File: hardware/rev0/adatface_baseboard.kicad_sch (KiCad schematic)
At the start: 89 parts, among them J1 Conn_01x06_Male, J2 Conn_02x32_Odd_Even, J3 Conn_02x32_Odd_Even, J4 Connector_USB_C_Receptacle_US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, J5 Connector_USB_C_Receptacle_US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, J6 Conn_01x06_Male, J7 Conn_01x26_Male, J8 Conn_01x01_Male, J9 Conn_01x01_Male, U1 PLR135_T8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

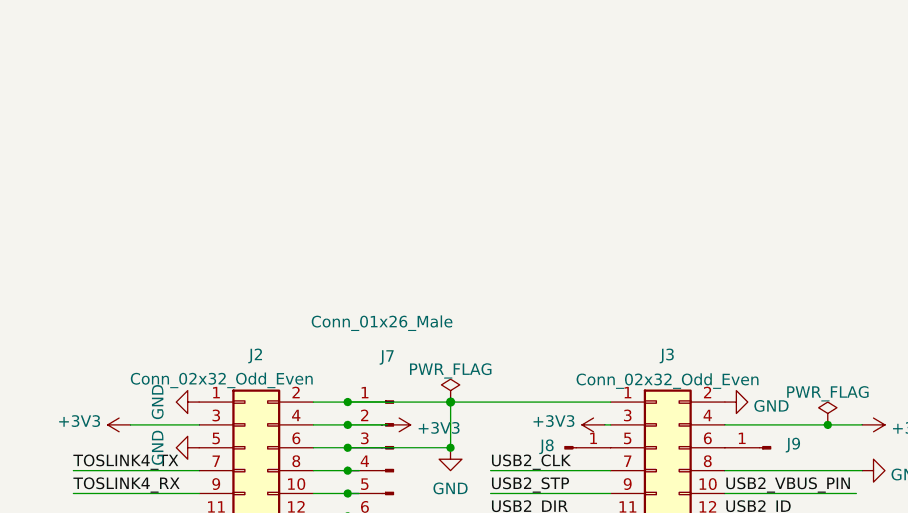
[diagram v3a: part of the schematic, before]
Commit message: baseboard rev0.1: Fix DRC rules with new KiCAD version, length matched USB PHY traces, more ground vias, fix trace spacing, ground headers
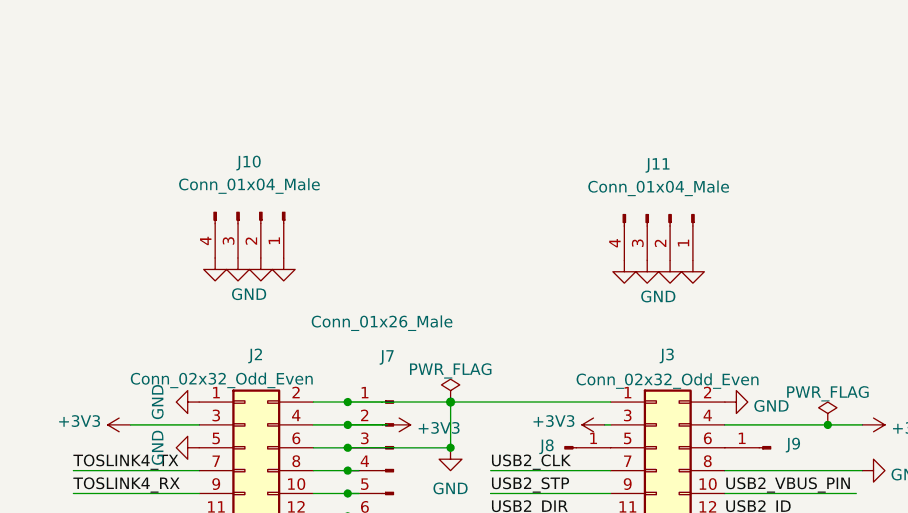
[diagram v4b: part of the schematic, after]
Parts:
- added J10, J11: Conn_01x04_Male, Connector_PinHeader_2.54mm:PinHeader_1x04_P2.54mm_Horizontal, symbol Connector:Conn_01x04_Male
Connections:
- net GND: now also J10.1 (Pin_1), J10.2 (Pin_2), J10.3 (Pin_3), J10.4 (Pin_4), J11.1 (Pin_1), J11.2 (Pin_2), J11.3 (Pin_3), J11.4 (Pin_4)
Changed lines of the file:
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@@
     )
   )
+  (symbol (lib_id "power:GND") (at 145.288 37.338 0) (unit 1)
+    (in_bom yes) (on_board yes)
+    (property "Reference" "#PWR034" (id 0) (at 145.288 43.688 0)
+      (effects (font (size 1.27 1.27)) hide)
+    )
+    (property "Value" "GND" (id 1) (at 144.526 41.402 0)
+      (effects (font (size 1.27 1.27)) (justify left))
+    )
+    (property "Footprint" "" (id 2) (at 145.288 37.338 0)
+      (effects (font (size 1.27 1.27)) hide)
+    )
+    (property "Datasheet" "" (id 3) (at 145.288 37.338 0)
+      (effects (font (size 1.27 1.27)) hide)
+    )
+    (pin "1")
+  )
   (symbol (lib_id "power:GND") (at 250.19 87.63 0) (unit 1)
     (in_bom yes) (on_board yes)
@@
     (pin "1")
   )
+  (symbol (lib_id "power:GND") (at 142.748 37.338 0) (unit 1)
+    (in_bom yes) (on_board yes)
+    (property "Reference" "#PWR033" (id 0) (at 142.748 43.688 0)
+      (effects (font (size 1.27 1.27)) hide)
+    )
+    (property "Value" "GND" (id 1) (at 140.716 41.402 0)
+      (effects (font (size 1.27 1.27)) (justify left) hide)
+    )
+    (property "Footprint" "" (id 2) (at 142.748 37.338 0)
+      (effects (font (size 1.27 1.27)) hide)
+    )
+    (property "Datasheet" "" (id 3) (at 142.748 37.338 0)
+      (effects (font (size 1.27 1.27)) hide)
+    )
+    (pin "1")
+  )
   (symbol (lib_id "power:GND") (at 140.97 53.34 270) (unit 1)
     (in_bom yes) (on_board yes)
@@
     (pin "1")
   )
+  (symbol (lib_id "power:GND") (at 150.368 37.338 0) (unit 1)
+    (in_bom yes) (on_board yes)
+    (property "Reference" "#PWR036" (id 0) (at 150.368 43.688 0)
+      (effects (font (size 1.27 1.27)) hide)
+    )
+    (property "Value" "GND" (id 1) (at 148.336 41.402 0)
+      (effects (font (size 1.27 1.27)) (justify left) hide)
+    )
+    (property "Footprint" "" (id 2) (at 150.368 37.338 0)
+      (effects (font (size 1.27 1.27)) hide)
+    )
+    (property "Datasheet" "" (id 3) (at 150.368 37.338 0)
+      (effects (font (size 1.27 1.27)) hide)
+    )
+    (pin "1")
+  )
   (symbol (lib_id "Connector_Generic:Conn_02x32_Odd_Even") (at 191.77 91.44 0) (unit 1)
     (in_bom yes) (on_board yes) (fields_autoplaced)
@@
     (pin "2")
   )
+  (symbol (lib_id "power:GND") (at 147.828 37.338 0) (unit 1)
+    (in_bom yes) (on_board yes)
+    (property "Reference" "#PWR035" (id 0) (at 147.828 43.688 0)
+      (effects (font (size 1.27 1.27)) hide)
+    )
+    (property "Value" "GND" (id 1) (at 145.796 41.402 0)
+      (effects (font (size 1.27 1.27)) (justify left) hide)
+    )
+    (property "Footprint" "" (id 2) (at 147.828 37.338 0)
+      (effects (font (size 1.27 1.27)) hide)
+    )
+    (property "Datasheet" "" (id 3) (at 147.828 37.338 0)
+      (effects (font (size 1.27 1.27)) hide)
+    )
+    (pin "1")
+  )
   (symbol (lib_id "Device:R_Small") (at 245.11 173.99 270) (unit 1)
     (in_bom yes) (on_board yes)
@@
     (pin "1")
   )
+  (symbol (lib_id "power:GND") (at 188.214 37.592 0) (unit 1)
+    (in_bom yes) (on_board yes)
+    (property "Reference" "#PWR037" (id 0) (at 188.214 43.942 0)
+      (effects (font (size 1.27 1.27)) hide)
+    )
+    (property "Value" "GND" (id 1) (at 186.182 41.656 0)
+      (effects (font (size 1.27 1.27)) (justify left) hide)
+    )
+    (property "Footprint" "" (id 2) (at 188.214 37.592 0)
+      (effects (font (size 1.27 1.27)) hide)
+    )
+    (property "Datasheet" "" (id 3) (at 188.214 37.592 0)
+      (effects (font (size 1.27 1.27)) hide)
+    )
+    (pin "1")
+  )
   (symbol (lib_id "Connector:TestPoint") (at 374.65 173.99 270) (unit 1)
     (in_bom yes) (on_board yes) (fields_autoplaced)
@@
     (pin "1")
   )
+  (symbol (lib_id "power:GND") (at 193.294 37.592 0) (unit 1)
+    (in_bom yes) (on_board yes)
+    (property "Reference" "#PWR039" (id 0) (at 193.294 43.942 0)
+      (effects (font (size 1.27 1.27)) hide)
+    )
+    (property "Value" "GND" (id 1) (at 191.262 41.656 0)
+      (effects (font (size 1.27 1.27)) (justify left) hide)
+    )
+    (property "Footprint" "" (id 2) (at 193.294 37.592 0)
+      (effects (font (size 1.27 1.27)) hide)
+    )
+    (property "Datasheet" "" (id 3) (at 193.294 37.592 0)
+      (effects (font (size 1.27 1.27)) hide)
+    )
+    (pin "1")
+  )
   (symbol (lib_id "Device:C_Small") (at 278.13 90.17 180) (unit 1)
     (in_bom yes) (on_board yes)
@@
     (pin "S1")
   )
+  (symbol (lib_id "power:GND") (at 195.834 37.592 0) (unit 1)
+    (in_bom yes) (on_board yes)
+    (property "Reference" "#PWR040" (id 0) (at 195.834 43.942 0)
+      (effects (font (size 1.27 1.27)) hide)
+    )
+    (property "Value" "GND" (id 1) (at 193.802 41.656 0)
+      (effects (font (size 1.27 1.27)) (justify left) hide)
+    )
+    (property "Footprint" "" (id 2) (at 195.834 37.592 0)
+      (effects (font (size 1.27 1.27)) hide)
+    )
+    (property "Datasheet" "" (id 3) (at 195.834 37.592 0)
+      (effects (font (size 1.27 1.27)) hide)
+    )
+    (pin "1")
+  )
   (symbol (lib_id "Device:LED_Small") (at 251.46 173.99 180) (unit 1)
     (in_bom yes) (on_board yes)
@@
     (pin "2")
   )
+  (symbol (lib_id "Connector:Conn_01x04_Male") (at 193.294 32.512 270) (unit 1)
+    (in_bom yes) (on_board yes) (fields_autoplaced)
+    (property "Reference" "J11" (id 0) (at 192.024 26.924 90))
+    (property "Value" "Conn_01x04_Male" (id 1) (at 192.024 29.464 90))
+    (property "Footprint" "Connector_PinHeader_2.54mm:PinHeader_1x04_P2.54mm_Horizontal" (id 2) (at 193.294 32.512 0)
+      (effects (font (size 1.27 1.27)) hide)
+    )
+    (property "Datasheet" "~" (id 3) (at 193.294 32.512 0)
+      (effects (font (size 1.27 1.27)) hide)
+    )
+    (pin "1")
+    (pin "2")
+    (pin "3")
+    (pin "4")
+  )
+  (symbol (lib_id "Connector:Conn_01x04_Male") (at 147.828 32.258 270) (unit 1)
+    (in_bom yes) (on_board yes) (fields_autoplaced)
+    (property "Reference" "J10" (id 0) (at 146.558 26.67 90))
+    (property "Value" "Conn_01x04_Male" (id 1) (at 146.558 29.21 90))
+    (property "Footprint" "Connector_PinHeader_2.54mm:PinHeader_1x04_P2.54mm_Horizontal" (id 2) (at 147.828 32.258 0)
+      (effects (font (size 1.27 1.27)) hide)
+    )
+    (property "Datasheet" "~" (id 3) (at 147.828 32.258 0)
+      (effects (font (size 1.27 1.27)) hide)
+    )
+    (pin "1")
+    (pin "2")
+    (pin "3")
+    (pin "4")
+  )
   (symbol (lib_id "power:+3V3") (at 104.14 26.67 0) (unit 1)
     (in_bom yes) (on_board yes)
@@
     (pin "1")
   )
+  (symbol (lib_id "power:GND") (at 190.754 37.592 0) (unit 1)
+    (in_bom yes) (on_board yes)
+    (property "Reference" "#PWR038" (id 0) (at 190.754 43.942 0)
+      (effects (font (size 1.27 1.27)) hide)
+    )
+    (property "Value" "GND" (id 1) (at 189.992 41.656 0)
+      (effects (font (size 1.27 1.27)) (justify left))
+    )
+    (property "Footprint" "" (id 2) (at 190.754 37.592 0)
+      (effects (font (size 1.27 1.27)) hide)
+    )
+    (property "Datasheet" "" (id 3) (at 190.754 37.592 0)
+      (effects (font (size 1.27 1.27)) hide)
+    )
+    (pin "1")
+  )
   (symbol (lib_id "power:GND") (at 274.32 92.71 0) (unit 1)
     (in_bom yes) (on_board yes)
@@
       (reference "#PWR032") (unit 1) (value "GND") (footprint "")
     )
+    (path "/26407b21-54ac-4400-bd7a-f92d85bcd44b"
+      (reference "#PWR033") (unit 1) (value "GND") (footprint "")
+    )
+    (path "/1fb9eddd-a1c5-4739-be2c-db47ae4c4311"
+      (reference "#PWR034") (unit 1) (value "GND") (footprint "")
+    )
+    (path "/43856b41-4b23-4930-8915-94498277d93f"
+      (reference "#PWR035") (unit 1) (value "GND") (footprint "")
+    )
+    (path "/38c0badc-867c-479d-abc4-08499734b765"
+      (reference "#PWR036") (unit 1) (value "GND") (footprint "")
+    )
+    (path "/74656f61-a940-45d1-8b0e-4b9d021f8cc7"
+      (reference "#PWR037") (unit 1) (value "GND") (footprint "")
+    )
+    (path "/bf7b3dee-e5b6-4cf1-8c34-7a74a459fc6c"
+      (reference "#PWR038") (unit 1) (value "GND") (footprint "")
+    )
+    (path "/7ed679e3-0863-480c-8a05-cfb55098302f"
+      (reference "#PWR039") (unit 1) (value "GND") (footprint "")
+    )
+    (path "/8e134283-ef54-4e7b-86e5-b730ed2958b9"
+      (reference "#PWR040") (unit 1) (value "GND") (footprint "")
+    )
     (path "/f1a89bc0-5244-4de8-b6c9-4d57a5cda268"
       (reference "#PWR0101") (unit 1) (value "+3V3") (footprint "")
@@
       (reference "J9") (unit 1) (value "Conn_01x01_Male") (footprint "Connector_PinHeader_2.54mm:PinHeader_1x01_P2.54mm_Horizontal")
     )
+    (path "/aac52934-1c85-45bd-bb3c-928245db964e"
+      (reference "J10") (unit 1) (value "Conn_01x04_Male") (footprint "Connector_PinHeader_2.54mm:PinHeader_1x04_P2.54mm_Horizontal")
+    )
+    (path "/aaae279b-4901-45fe-8963-5ed1674eb265"
+      (reference "J11") (unit 1) (value "Conn_01x04_Male") (footprint "Connector_PinHeader_2.54mm:PinHeader_1x04_P2.54mm_Horizontal")
+    )
     (path "/5448f638-8d6b-4093-912f-b251fcd810b2"
